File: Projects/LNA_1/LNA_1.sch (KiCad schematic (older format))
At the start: 26 parts, among them J1 SMA-J-P-H-ST-EM1, J2 SMA-J-P-H-ST-EM1, Q2 BFR193, U1 BFU790F

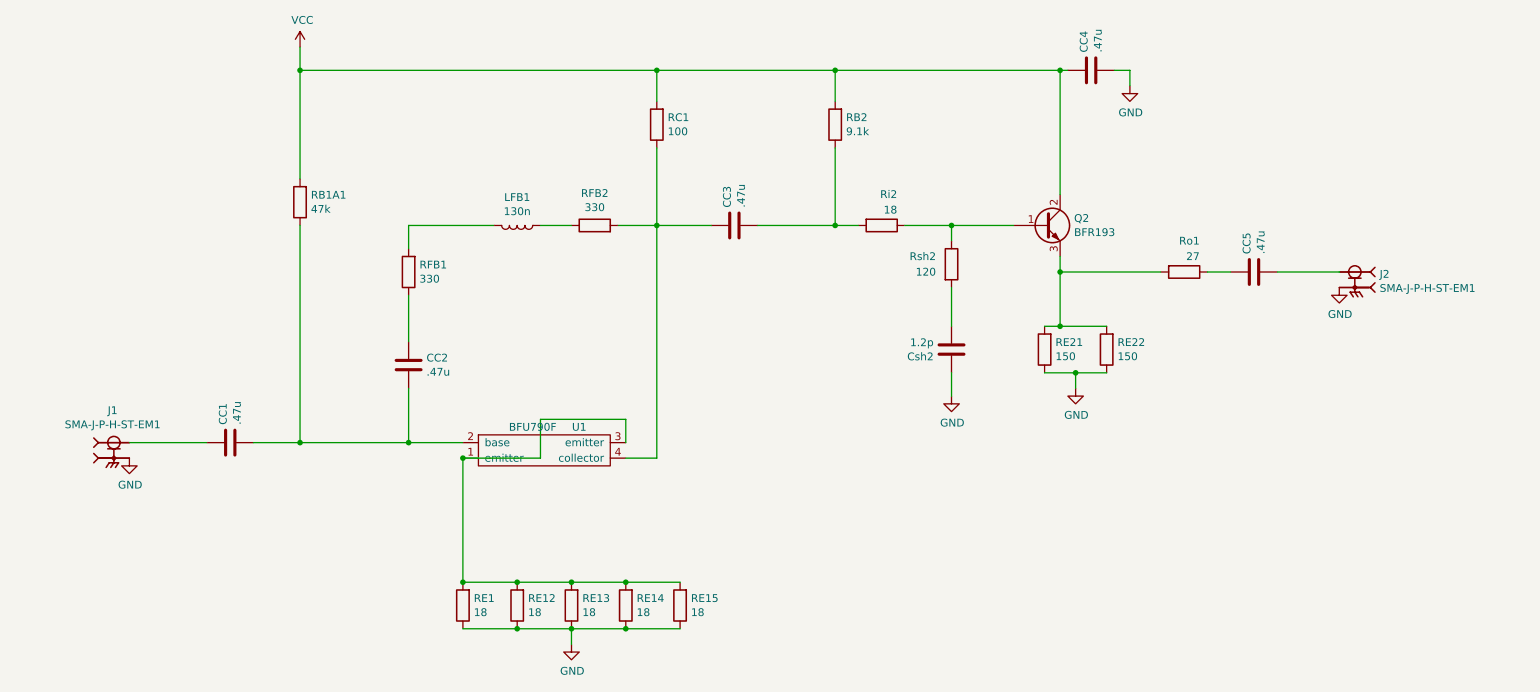
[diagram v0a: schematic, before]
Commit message: fixed SMA connectors
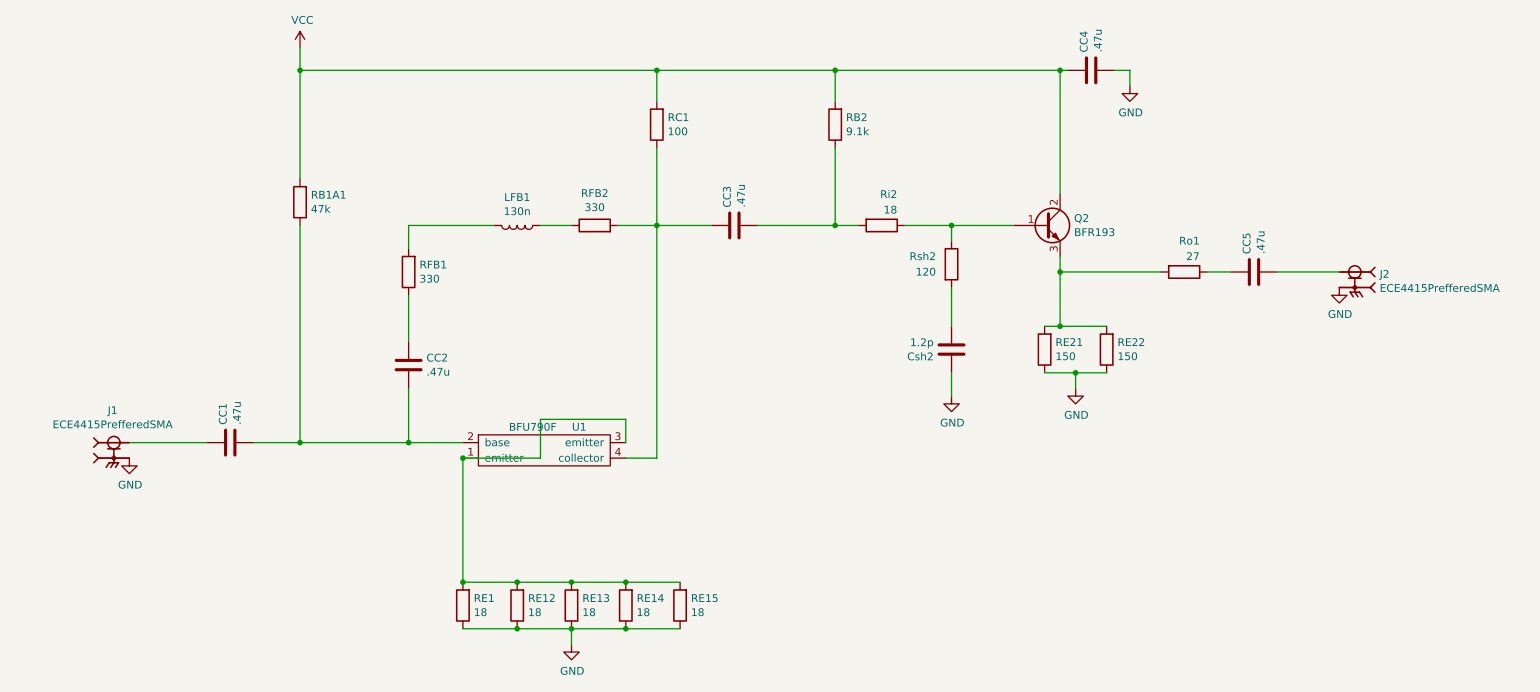
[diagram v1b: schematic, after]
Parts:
- removed J1, J2: SMA-J-P-H-ST-EM1, SAMTEC_SMA-J-P-H-ST-EM1, symbol RandomSMAIFoundOnline:SMA-J-P-H-ST-EM1
- added J1, J2: ECE4415PrefferedSMA, AdditionalLibs:ECE4415PrefferedSMA, symbol AdditionalParts:ECE4415PrefferedSMA
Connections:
- net GND: now also J1.S1, J1.S2, J1.S3, J1.S4, J2.S1, J2.S2, J2.S3, J2.S4
- net at CC1.1: now also J1.1
- net at CC5.2: now also J2.1
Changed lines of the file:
@@
 $EndComp
 $Comp
-L RandomSMAIFoundOnline:SMA-J-P-H-ST-EM1 J1
-U 1 1 60099154
+L AdditionalParts:ECE4415PrefferedSMA J1
+U 1 1 6010B5E4
 P 2200 4000
 F 0 "J1" H 2192 4307 50  0000 C CNN
-F 1 "SMA-J-P-H-ST-EM1" H 2192 4216 50  0000 C CNN
-F 2 "SAMTEC_SMA-J-P-H-ST-EM1" H 2200 4000 50  0001 L BNN
+F 1 "ECE4415PrefferedSMA" H 2192 4216 50  0000 C CNN
+F 2 "AdditionalLibs:ECE4415PrefferedSMA" H 2200 4000 50  0001 L BNN
 F 3 "" H 2200 4000 50  0001 L BNN
-F 4 "Samtec" H 2200 4000 50  0001 L BNN "MANUFACTURER"
-F 5 "G" H 2200 4000 50  0001 L BNN "PARTREV"
-F 6 "Manufacturer Recommendations" H 2200 4000 50  0001 L BNN "STANDARD"
-F 7 "3.675mm" H 2200 4000 50  0001 L BNN "MAXIMUM_PACKAGE_HEIGHT"
+F 4 "Manufacturer Recommendations" H 2200 4000 50  0001 L BNN "STANDARD"
+F 5 "8.052 mm" H 2200 4000 50  0001 L BNN "MAXIMUM_PACKAGE_HEIGHT"
+F 6 "Cinch Connectivity" H 2200 4000 50  0001 L BNN "MANUFACTURER"
+F 7 "5" H 2200 4000 50  0001 L BNN "PARTREV"
 	1    2200 4000
 	1    0    0    -1
 $EndComp
 $Comp
-L RandomSMAIFoundOnline:SMA-J-P-H-ST-EM1 J2
-U 1 1 6009B843
+L AdditionalParts:ECE4415PrefferedSMA J2
+U 1 1 6010D782
 P 10200 2900
 F 0 "J2" H 10040 2986 50  0000 R CNN
-F 1 "SMA-J-P-H-ST-EM1" H 10040 2895 50  0000 R CNN
-F 2 "SAMTEC_SMA-J-P-H-ST-EM1" H 10200 2900 50  0001 L BNN
+F 1 "ECE4415PrefferedSMA" H 10040 2895 50  0000 R CNN
+F 2 "AdditionalLibs:ECE4415PrefferedSMA" H 10200 2900 50  0001 L BNN
 F 3 "" H 10200 2900 50  0001 L BNN
-F 4 "Samtec" H 10200 2900 50  0001 L BNN "MANUFACTURER"
-F 5 "G" H 10200 2900 50  0001 L BNN "PARTREV"
-F 6 "Manufacturer Recommendations" H 10200 2900 50  0001 L BNN "STANDARD"
-F 7 "3.675mm" H 10200 2900 50  0001 L BNN "MAXIMUM_PACKAGE_HEIGHT"
+F 4 "Manufacturer Recommendations" H 10200 2900 50  0001 L BNN "STANDARD"
+F 5 "8.052 mm" H 10200 2900 50  0001 L BNN "MAXIMUM_PACKAGE_HEIGHT"
+F 6 "Cinch Connectivity" H 10200 2900 50  0001 L BNN "MANUFACTURER"
+F 7 "5" H 10200 2900 50  0001 L BNN "PARTREV"
 	1    10200 2900
 	-1   0    0    -1

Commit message: added via stitching to the boards and changed to a barrel jack on the LNA
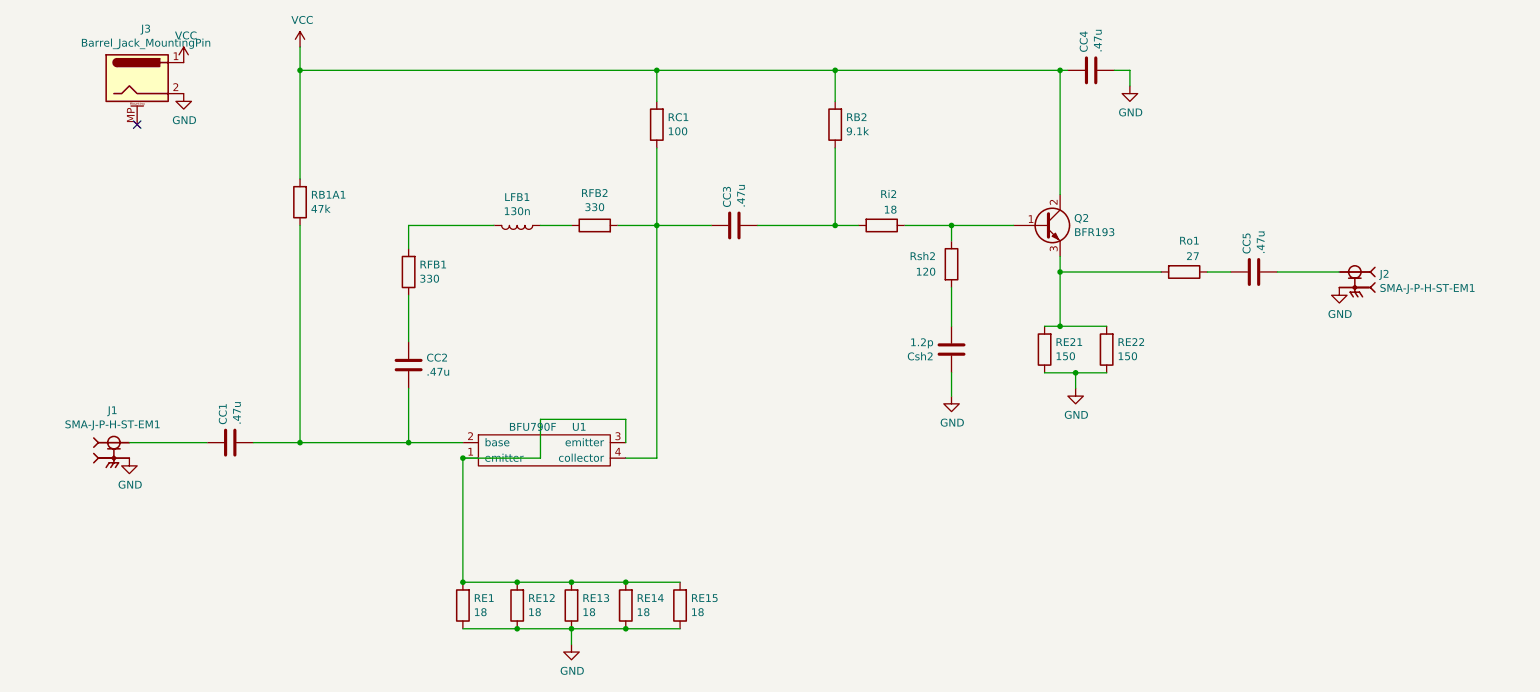
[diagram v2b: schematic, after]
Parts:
- removed J1, J2: ECE4415PrefferedSMA, AdditionalLibs:ECE4415PrefferedSMA, symbol AdditionalParts:ECE4415PrefferedSMA
- added J1, J2: SMA-J-P-H-ST-EM1, SAMTEC_SMA-J-P-H-ST-EM1, symbol RandomSMAIFoundOnline:SMA-J-P-H-ST-EM1
- added J3: Barrel_Jack_MountingPin, Connector_BarrelJack:BarrelJack_Horizontal, symbol Connector:Barrel_Jack_MountingPin
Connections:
- net GND: now also J1.2_1, J1.2_2, J1.3_1, J1.3_2, J2.2_1, J2.2_2, J2.3_1, J2.3_2, J3.2
- net VCC: now also J3.1
- net at CC1.1: now also J1.1
- net at CC5.2: now also J2.1
- no-connect marks 0 -> 1
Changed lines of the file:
@@
 $EndComp
 $Comp
-L AdditionalParts:ECE4415PrefferedSMA J1
-U 1 1 6010B5E4
+L power:VCC #PWR0108
+U 1 1 600FAC3B
+P 2650 1450
+F 0 "#PWR0108" H 2650 1300 50  0001 C CNN
+F 1 "VCC" H 2665 1623 50  0000 C CNN
+F 2 "" H 2650 1450 50  0001 C CNN
+F 3 "" H 2650 1450 50  0001 C CNN
+	1    2650 1450
+	1    0    0    -1
+$EndComp
+$Comp
+L power:GND #PWR0109
+U 1 1 600FB0E8
+P 2650 1650
+F 0 "#PWR0109" H 2650 1400 50  0001 C CNN
+F 1 "GND" H 2655 1477 50  0000 C CNN
+F 2 "" H 2650 1650 50  0001 C CNN
+F 3 "" H 2650 1650 50  0001 C CNN
+	1    2650 1650
+	1    0    0    -1
+$EndComp
+$Comp
+L Connector:Barrel_Jack_MountingPin J3
+U 1 1 60111861
+P 2350 1550
+F 0 "J3" H 2407 1867 50  0000 C CNN
+F 1 "Barrel_Jack_MountingPin" H 2407 1776 50  0000 C CNN
+F 2 "Connector_BarrelJack:BarrelJack_Horizontal" H 2400 1510 50  0001 C CNN
+F 3 "~" H 2400 1510 50  0001 C CNN
+	1    2350 1550
+	1    0    0    -1
+$EndComp
+NoConn ~ 2350 1850
+$Comp
+L RandomSMAIFoundOnline:SMA-J-P-H-ST-EM1 J1
+U 1 1 60135EC5
 P 2200 4000
 F 0 "J1" H 2192 4307 50  0000 C CNN
-F 1 "ECE4415PrefferedSMA" H 2192 4216 50  0000 C CNN
-F 2 "AdditionalLibs:ECE4415PrefferedSMA" H 2200 4000 50  0001 L BNN
+F 1 "SMA-J-P-H-ST-EM1" H 2192 4216 50  0000 C CNN
+F 2 "SAMTEC_SMA-J-P-H-ST-EM1" H 2200 4000 50  0001 L BNN
 F 3 "" H 2200 4000 50  0001 L BNN
-F 4 "Manufacturer Recommendations" H 2200 4000 50  0001 L BNN "STANDARD"
-F 5 "8.052 mm" H 2200 4000 50  0001 L BNN "MAXIMUM_PACKAGE_HEIGHT"
-F 6 "Cinch Connectivity" H 2200 4000 50  0001 L BNN "MANUFACTURER"
-F 7 "5" H 2200 4000 50  0001 L BNN "PARTREV"
+F 4 "Samtec" H 2200 4000 50  0001 L BNN "MANUFACTURER"
+F 5 "G" H 2200 4000 50  0001 L BNN "PARTREV"
+F 6 "Manufacturer Recommendations" H 2200 4000 50  0001 L BNN "STANDARD"
+F 7 "3.675mm" H 2200 4000 50  0001 L BNN "MAXIMUM_PACKAGE_HEIGHT"
 	1    2200 4000
 	1    0    0    -1
 $EndComp
 $Comp
-L AdditionalParts:ECE4415PrefferedSMA J2
-U 1 1 6010D782
+L RandomSMAIFoundOnline:SMA-J-P-H-ST-EM1 J2
+U 1 1 6013753B
 P 10200 2900
 F 0 "J2" H 10040 2986 50  0000 R CNN
-F 1 "ECE4415PrefferedSMA" H 10040 2895 50  0000 R CNN
-F 2 "AdditionalLibs:ECE4415PrefferedSMA" H 10200 2900 50  0001 L BNN
+F 1 "SMA-J-P-H-ST-EM1" H 10040 2895 50  0000 R CNN
+F 2 "SAMTEC_SMA-J-P-H-ST-EM1" H 10200 2900 50  0001 L BNN
 F 3 "" H 10200 2900 50  0001 L BNN
-F 4 "Manufacturer Recommendations" H 10200 2900 50  0001 L BNN "STANDARD"
-F 5 "8.052 mm" H 10200 2900 50  0001 L BNN "MAXIMUM_PACKAGE_HEIGHT"
-F 6 "Cinch Connectivity" H 10200 2900 50  0001 L BNN "MANUFACTURER"
-F 7 "5" H 10200 2900 50  0001 L BNN "PARTREV"
+F 4 "Samtec" H 10200 2900 50  0001 L BNN "MANUFACTURER"
+F 5 "G" H 10200 2900 50  0001 L BNN "PARTREV"
+F 6 "Manufacturer Recommendations" H 10200 2900 50  0001 L BNN "STANDARD"
+F 7 "3.675mm" H 10200 2900 50  0001 L BNN "MAXIMUM_PACKAGE_HEIGHT"
 	1    10200 2900
 	-1   0    0    -1

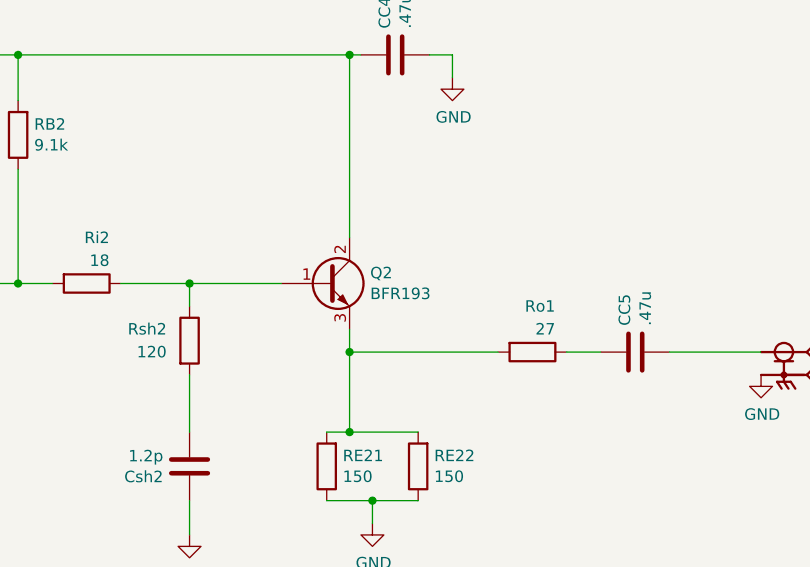
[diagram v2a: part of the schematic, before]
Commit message: fixed the BF193 on the LNA was in wrong orientation
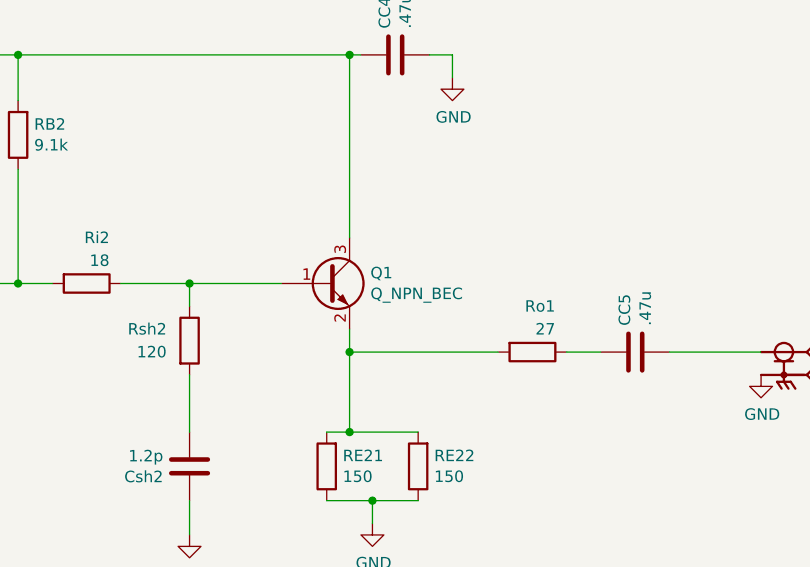
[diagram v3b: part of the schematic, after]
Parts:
- removed Q2: BFR193, Package_TO_SOT_SMD:SOT-23, symbol Device:Q_NPN_BCE
- added Q1: Q_NPN_BEC, Package_TO_SOT_SMD:SOT-323_SC-70, symbol Device:Q_NPN_BEC
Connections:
- net VCC: now also Q1.3 (C)
- net at Ri2.1, Rsh2.1: now also Q1.1 (B)
- net at RE21.2, RE22.2, Ro1.2: now also Q1.2 (E)
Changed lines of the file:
@@
 	-1   0    0    1
-$EndComp
-$Comp
-L Device:Q_NPN_BCE Q2
-U 1 1 600D76BD
-P 8200 2500
-F 0 "Q2" H 8390 2546 50  0000 L CNN
-F 1 "BFR193" H 8390 2455 50  0000 L CNN
-F 2 "Package_TO_SOT_SMD:SOT-23" H 8400 2600 50  0001 C CNN
-F 3 "~" H 8200 2500 50  0001 C CNN
-	1    8200 2500
-	1    0    0    -1
 $EndComp
 Wire Wire Line
@@
 	-1   0    0    -1
 $EndComp
+$Comp
+L Device:Q_NPN_BEC Q1
+U 1 1 60109097
+P 8200 2500
+F 0 "Q1" H 8391 2546 50  0000 L CNN
+F 1 "Q_NPN_BEC" H 8391 2455 50  0000 L CNN
+F 2 "Package_TO_SOT_SMD:SOT-323_SC-70" H 8400 2600 50  0001 C CNN
+F 3 "~" H 8200 2500 50  0001 C CNN
+	1    8200 2500
+	1    0    0    -1
+$EndComp
 $EndSCHEMATC

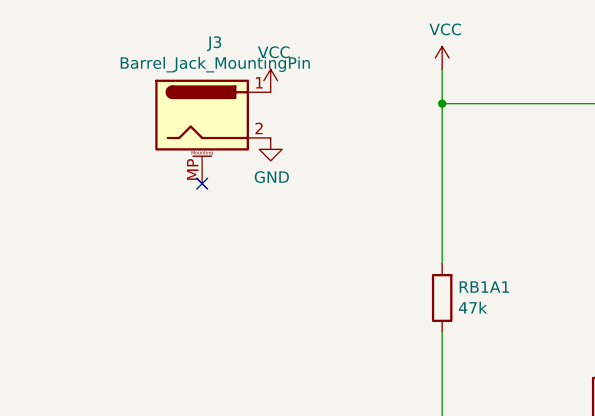
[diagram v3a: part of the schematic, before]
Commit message: added tantalum 10uF cap to the power supply
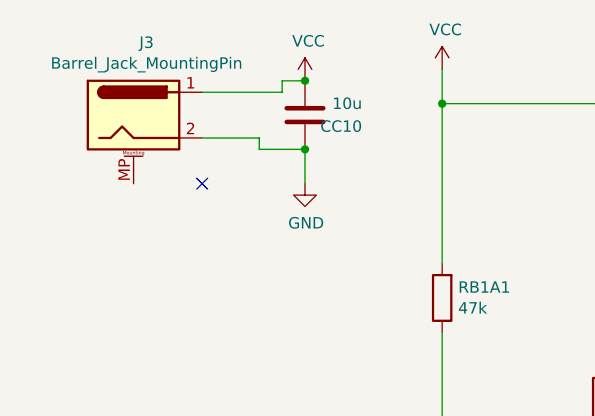
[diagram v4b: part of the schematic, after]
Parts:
- added CC10: 10u, Capacitor_SMD:C_0805_2012Metric, symbol Device:C
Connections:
- net GND: now also CC10.1
- net VCC: now also CC10.2
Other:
- moved on the sheet: J3
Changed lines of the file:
@@
 L power:VCC #PWR0108
 U 1 1 600FAC3B
-P 2650 1450
-F 0 "#PWR0108" H 2650 1300 50  0001 C CNN
-F 1 "VCC" H 2665 1623 50  0000 C CNN
-F 2 "" H 2650 1450 50  0001 C CNN
-F 3 "" H 2650 1450 50  0001 C CNN
-	1    2650 1450
+P 2800 1400
+F 0 "#PWR0108" H 2800 1250 50  0001 C CNN
+F 1 "VCC" H 2815 1573 50  0000 C CNN
+F 2 "" H 2800 1400 50  0001 C CNN
+F 3 "" H 2800 1400 50  0001 C CNN
+	1    2800 1400
 	1    0    0    -1
 $EndComp
@@
 L power:GND #PWR0109
 U 1 1 600FB0E8
-P 2650 1650
-F 0 "#PWR0109" H 2650 1400 50  0001 C CNN
-F 1 "GND" H 2655 1477 50  0000 C CNN
-F 2 "" H 2650 1650 50  0001 C CNN
-F 3 "" H 2650 1650 50  0001 C CNN
-	1    2650 1650
+P 2800 1850
+F 0 "#PWR0109" H 2800 1600 50  0001 C CNN
+F 1 "GND" H 2805 1677 50  0000 C CNN
+F 2 "" H 2800 1850 50  0001 C CNN
+F 3 "" H 2800 1850 50  0001 C CNN
+	1    2800 1850
 	1    0    0    -1
 $EndComp
@@
 L Connector:Barrel_Jack_MountingPin J3
 U 1 1 60111861
-P 2350 1550
-F 0 "J3" H 2407 1867 50  0000 C CNN
-F 1 "Barrel_Jack_MountingPin" H 2407 1776 50  0000 C CNN
-F 2 "Connector_BarrelJack:BarrelJack_Horizontal" H 2400 1510 50  0001 C CNN
-F 3 "~" H 2400 1510 50  0001 C CNN
-	1    2350 1550
+P 2050 1550
+F 0 "J3" H 2107 1867 50  0000 C CNN
+F 1 "Barrel_Jack_MountingPin" H 2107 1776 50  0000 C CNN
+F 2 "Connector_BarrelJack:BarrelJack_Horizontal" H 2100 1510 50  0001 C CNN
+F 3 "~" H 2100 1510 50  0001 C CNN
+	1    2050 1550
 	1    0    0    -1
 $EndComp
@@
 	1    0    0    -1
 $EndComp
+Wire Wire Line
+	2700 1450 2700 1400
+Wire Wire Line
+	2700 1400 2800 1400
+$Comp
+L Device:C CC10
+U 1 1 6010E877
+P 2800 1550
+F 0 "CC10" H 2550 1600 50  0000 L CNN
+F 1 "10u" H 2550 1500 50  0000 L CNN
+F 2 "Capacitor_SMD:C_0805_2012Metric" H 2838 1400 50  0001 C CNN
+F 3 "~" H 2800 1550 50  0001 C CNN
+	1    2800 1550
+	-1   0    0    1
+$EndComp
+Connection ~ 2800 1400
+Wire Wire Line
+	2350 1450 2700 1450
+Wire Wire Line
+	2350 1650 2600 1650
+Wire Wire Line
+	2600 1650 2600 1700
+Wire Wire Line
+	2600 1700 2800 1700
+Wire Wire Line
+	2800 1700 2800 1850
+Connection ~ 2800 1700
 $EndSCHEMATC

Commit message: Created a new file
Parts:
- CC10: footprint Capacitor_SMD:C_0805_2012Metric -> Capacitor_SMD:C_1206_3216Metric
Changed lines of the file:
@@
 F 0 "CC10" H 2550 1600 50  0000 L CNN
 F 1 "10u" H 2550 1500 50  0000 L CNN
-F 2 "Capacitor_SMD:C_0805_2012Metric" H 2838 1400 50  0001 C CNN
+F 2 "Capacitor_SMD:C_1206_3216Metric" H 2838 1400 50  0001 C CNN
 F 3 "~" H 2800 1550 50  0001 C CNN
 	1    2800 1550
